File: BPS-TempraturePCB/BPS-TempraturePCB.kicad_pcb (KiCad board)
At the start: 2 copper layers, 70.6 x 66.7 mm, 39 parts, among them J1 Conn_01x24_Female, J2 TEMPSPIANALYZER, U1 MIC5317-2.5xM5, U2 LM321, U3 ADS7953SBDBT

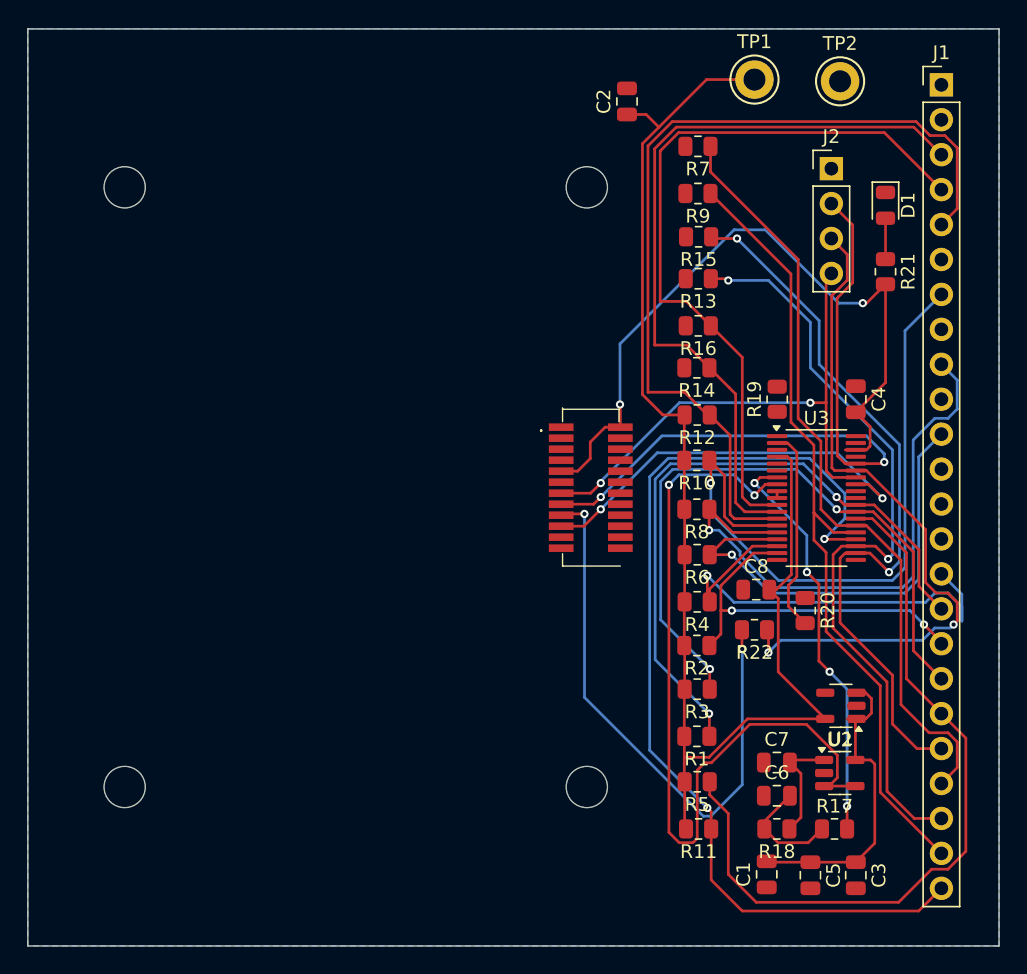
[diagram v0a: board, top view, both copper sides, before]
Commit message: All Traces connected. Need to fix silkscreen errors and add a few more test points
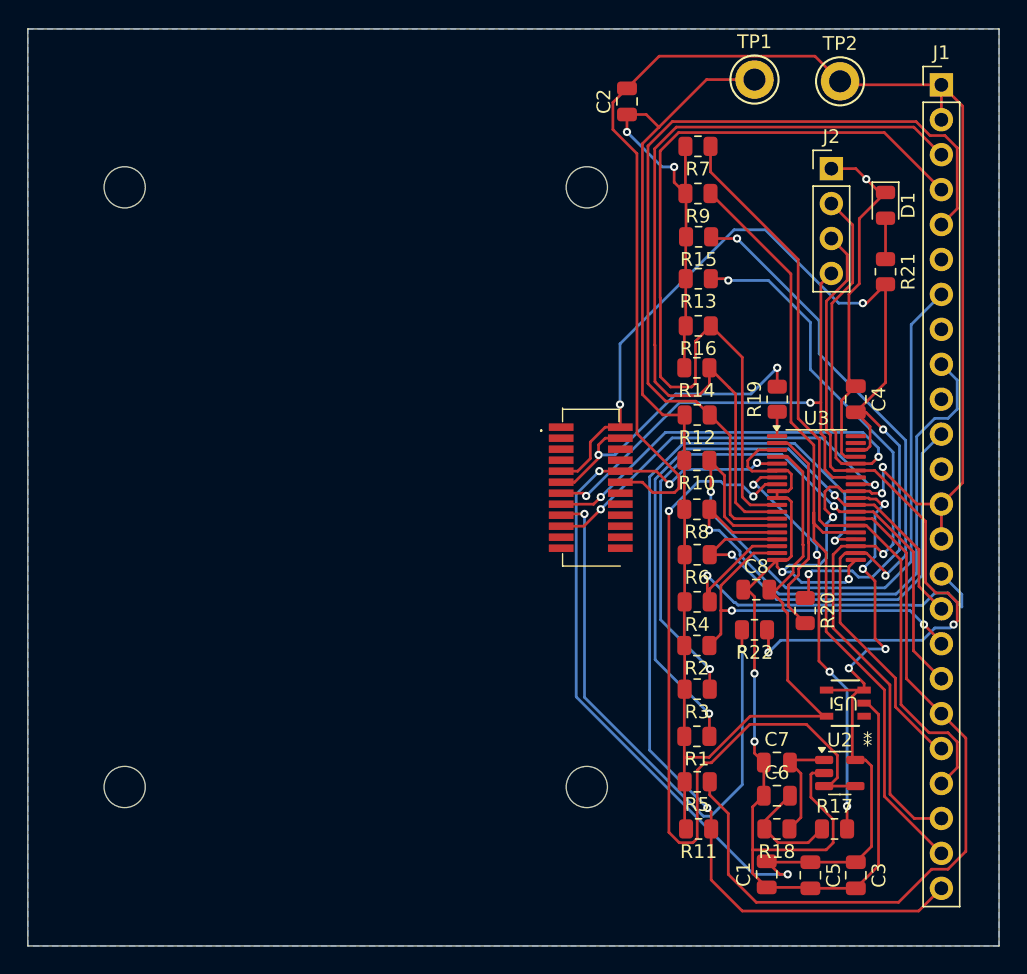
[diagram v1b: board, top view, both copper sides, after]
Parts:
- removed U1: MIC5317-2.5xM5, Package_TO_SOT_SMD:SOT-23-5
- added U5: REF4132B25DBVR, REF4132:SOT-23-5_DBV_TEX, F.Cu at (114.8, 106.7)
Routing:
- net GNDA: track 0.50 -> 202.3 mm, vias 0 -> 7
- net VDDA: track 23.6 -> 97.0 mm, vias 0 -> 8
- net GND: track 0.00 -> 49.7 mm, vias 0 -> 3
- net +2V5: track 99.0 -> 124.1 mm, vias 0 -> 2
- net +3.3V: track 52.9 -> 73.5 mm, vias 2 -> 4
- net /temp16: track 54.2 -> 62.9 mm
- net /temp15: track 55.1 -> 59.1 mm
- net /temp10: track 34.2 -> 32.3 mm
- net Net-(U3-GPIO2): track 0.00 -> 1.78 mm
- net /ADCIN: track 59.5 -> 58.0 mm
- net /SPI1_NSS: track 29.3 -> 28.3 mm
- net /temp1: track 47.5 -> 48.4 mm
- net /temp2: track 47.9 -> 48.8 mm
- net /temp8: track 54.4 -> 53.5 mm
- net Net-(U3-GPIO3): track 14.9 -> 15.6 mm
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
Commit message: added silkscreen for temprature pinheaders and testpoint for analog vdd and analog ground.
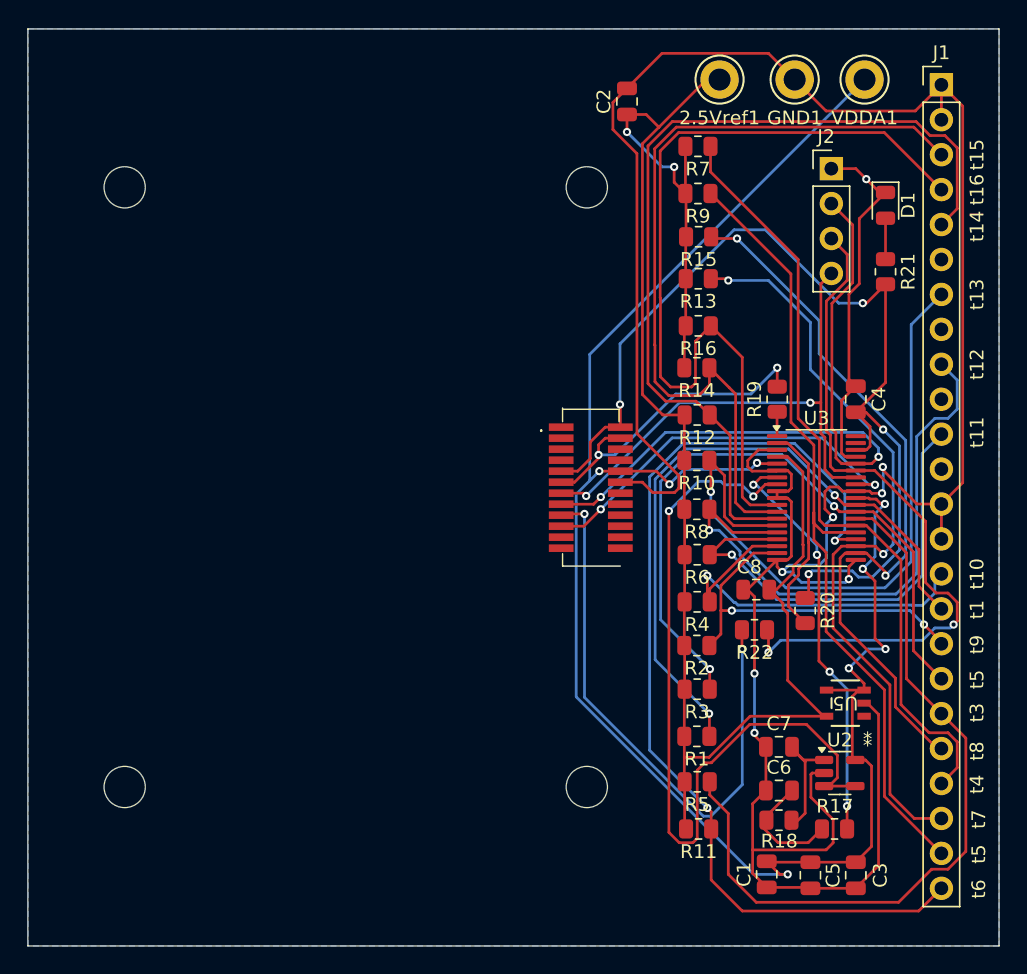
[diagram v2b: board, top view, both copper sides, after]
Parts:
- added VDDA1: TestPoint, TestPoint:TestPoint_Keystone_5005-5009_Compact, F.Cu at (116.2, 61.3)
- moved GND1 3.30 mm to (111.1, 61.3)
- moved 2.5Vref1 2.54 mm to (105.7, 61.3)
- moved C7 1.15 mm to (110.0, 109.9)
- moved R18 0.65 mm to (110.0, 115.2)
- moved C6 0.41 mm to (110.0, 113.0)
- renumbered TP1 to 2.5Vref1, TP2 to GND1
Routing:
- net VDDA: track 97.0 -> 134.5 mm
- net /temp10: track 32.3 -> 28.5 mm
- net +2V5: track 124.1 -> 121.6 mm
- net GNDA: track 202.3 -> 204.4 mm
- net Net-(U2-+): track 8.33 -> 9.65 mm
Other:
- board text added: "t1"
- board text added: "t10"
- board text added: "t11"
- board text added: "t12"
- board text added: "t13"
- board text added: "t14"
- board text added: "t15"
- board text added: "t16"
- board text added: "t3"
- board text added: "t4"
- board text added: "t5"
- board text added: "t6"
- board text added: "t7"
- board text added: "t8"
- board text added: "t9"

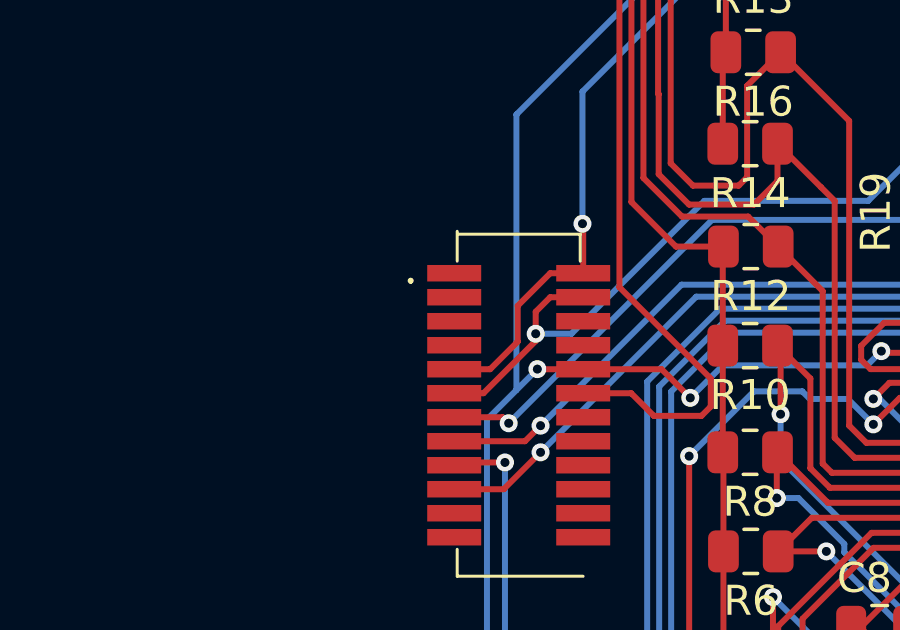
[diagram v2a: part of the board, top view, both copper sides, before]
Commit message: Fixed Missing ground connection
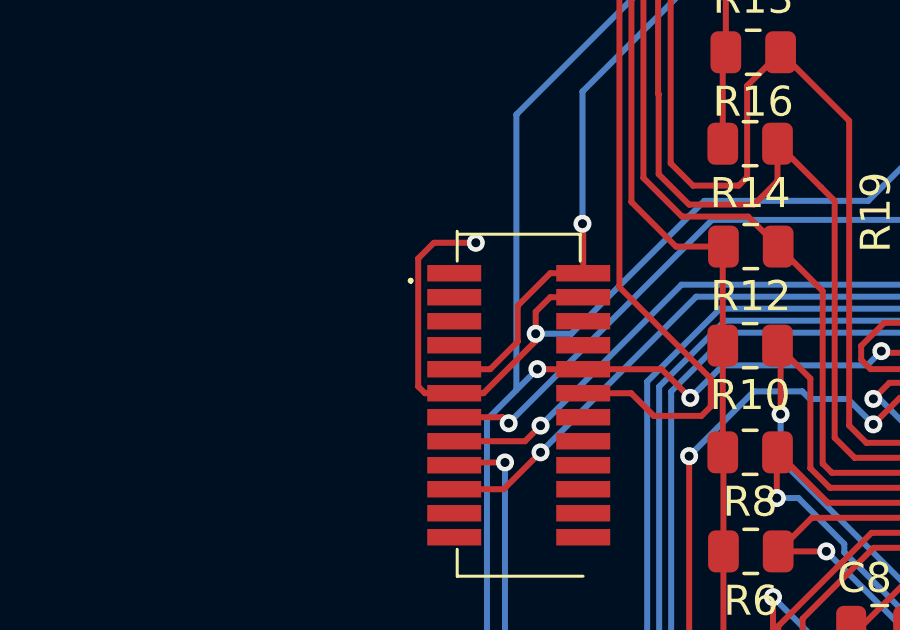
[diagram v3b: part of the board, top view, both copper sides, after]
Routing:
- net GND: track 49.7 -> 57.4 mm, vias 3 -> 4
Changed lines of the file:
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@@
+	)
+	(segment
+		(start 94.14926 90.61326)
+		(end 93.17426 90.61326)
+		(width 0.2)
+		(layer "F.Cu")
+		(net 5)
 	)
 	(segment
@@
 	)
 	(segment
+		(start 93.472 85.598)
+		(end 94.869 85.598)
+		(width 0.2)
+		(layer "F.Cu")
+		(net 5)
+	)
+	(segment
 		(start 115.070062 83.132062)
 		(end 115.070062 76.94231)
@@
 		(start 114.80009 88.766)
 		(end 114.5325 88.49841)
+		(width 0.2)
+		(layer "F.Cu")
+		(net 5)
+	)
+	(segment
+		(start 92.94926 90.38826)
+		(end 92.94926 86.12074)
 		(width 0.2)
 		(layer "F.Cu")
@@
 	)
 	(segment
+		(start 92.94926 86.12074)
+		(end 93.472 85.598)
+		(width 0.2)
+		(layer "F.Cu")
+		(net 5)
+	)
+	(segment
 		(start 115.57 88.766)
 		(end 114.80009 88.766)
+		(width 0.2)
+		(layer "F.Cu")
+		(net 5)
+	)
+	(segment
+		(start 93.17426 90.61326)
+		(end 92.94926 90.38826)
 		(width 0.2)
 		(layer "F.Cu")
@@
 		(size 0.6)
 		(drill 0.3)
+		(layers "F.Cu" "B.Cu")
+		(net 5)
+	)
+	(via
+		(at 94.869 85.598)
+		(size 0.6)
+		(drill 0.3)

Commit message: Redid routing to be better.
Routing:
- net /ADCIN: track 58.0 -> 27.6 mm
- net Net-(U4-SPI1_MOSI): track 42.3 -> 16.6 mm
- net GNDA: track 204.4 -> 180.3 mm, vias 7 -> 0
- net VDDA: track 134.5 -> 111.9 mm, vias 8 -> 4
- net /temp13: track 50.4 -> 31.8 mm
- net /temp5: track 59.8 -> 78.1 mm, vias 0 -> 2
- net /temp4: track 56.8 -> 74.7 mm
- net /temp3: track 55.1 -> 38.8 mm, vias 0 -> 1
- net /temp1: track 48.4 -> 32.6 mm, vias 2 -> 1
- net +3.3V: track 73.5 -> 59.0 mm, vias 4 -> 2
- net /temp15: track 59.1 -> 45.5 mm, vias 0 -> 2
- net /temp6: track 71.5 -> 58.1 mm, vias 2 -> 1
- net /temp11: track 33.7 -> 20.9 mm
- net /SPI1_NSS: track 28.3 -> 37.7 mm
- net GND: track 57.4 -> 66.3 mm, vias 4 -> 2
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- removed copper zone on B.Cu, net GND
